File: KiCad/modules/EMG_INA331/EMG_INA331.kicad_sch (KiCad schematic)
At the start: 34 parts, among them J10 Conn_01x01_Pin, J13 Conn_01x01_Pin, J14 Conn_01x01_Pin, J15 Conn_01x01_Pin, J6 Conn_01x01_Pin, J7 Conn_01x01_Pin, J8 Conn_01x01_Pin, J9 Conn_01x01_Pin, U1 TLV9044IPWR, U2 AP2112K-3.3TRG1, U3 INA350ABSIDSGR_C4370677

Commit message: INA331 IMUICM
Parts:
- removed C6: 1uF, Capacitor_SMD:C_0402_1005Metric, symbol Device:C
- removed R1, R10, R12, R14: R, Resistor_SMD:R_0201_0603Metric, symbol Device:R
- removed U1: TLV9044IPWR, 00_lcsc:TSSOP-14_L5.0-W4.4-P0.65-LS6.4-BL, symbol 00_lcsc:TLV9044IPWR
- removed U2: AP2112K-3.3TRG1, 00_custom-footprints:SOT95P285X140-5N, symbol 00_custom:AP2112K-3.3TRG1
- added C14: 100n, Capacitor_SMD:C_0402_1005Metric, symbol Device:C
- added C15: 1u, Capacitor_SMD:C_0402_1005Metric, symbol Device:C
- added C3: 10nF, Capacitor_SMD:C_0402_1005Metric, symbol Device:C
- added C7: 1uF, Capacitor_SMD:C_0402_1005Metric, symbol Device:C
- added C9: 100nF, Capacitor_SMD:C_0402_1005Metric, symbol Device:C
- added J10, J9: Conn_01x01_Pin, 00_custom-footprints:PinHeader_1x01_P1.27mm_Vertical, symbol Connector:Conn_01x01_Pin
- added R4, R5: 4k, Resistor_SMD:R_0402_1005Metric, symbol Device:R
- added R6, R7: 10k, Resistor_SMD:R_0402_1005Metric, symbol Device:R
- added TP1, TP2, TP3: TestPoint, 00_custom-footprints:TestPoint_Pad_D1.0mm, symbol 00_custom:TestPoint
- added U2, U4: OPA333, 00_lcsc:SOT-23-5_L2.9-W1.6-P0.95-LS2.8-BR, symbol 00_lcsc:OPA333M5_TR
- added U3: AP2112K-3.3TRG1, 00_lcsc:SOT-25-5_L2.9-W1.6-P0.95-LS2.8-BL, symbol 00_lcsc:AP2112K-3.3TRG1
- added U5: CJ432, 00_lcsc:SOT-23-3_L2.9-W1.3-P1.90-LS2.4-BR, symbol 00_lcsc:CJ432
- added U6: LIS3DHTR, 00_lcsc:LGA-16_L3.0-W3.0-P0.50-TL, symbol 00_lcsc:LIS3DHTR
- C1: renamed from C11; value 1uF -> 10uF
- C12: renamed from C1; value 1uF -> 100nF
- C2: renamed from C12; value 1uF -> 100nF
- C4, C5: value 1uF -> 100pF
- C5: footprint Capacitor_SMD:C_0201_0603Metric -> Capacitor_SMD:C_0402_1005Metric
- J10, J13, J14, J15, J6, J7, J8, J9: footprint Connector_PinHeader_1.27mm:PinHeader_1x01_P1.27mm_Vertical -> 00_custom-footprints:PinHeader_1x01_P1.27mm_Vertical
- R1: renamed from R5; value R -> 2k; footprint Resistor_SMD:R_0201_0603Metric -> Resistor_SMD:R_0402_1005Metric
- R10: renamed from R11; value R -> 1k; footprint Resistor_SMD:R_0201_0603Metric -> Resistor_SMD:R_0402_1005Metric
- R11: renamed from R9; value R -> 100k; footprint Resistor_SMD:R_0201_0603Metric -> Resistor_SMD:R_0402_1005Metric
- R12: renamed from R4; value R -> 1k; footprint Resistor_SMD:R_0201_0603Metric -> Resistor_SMD:R_0402_1005Metric
- R2: renamed from R3; value R -> 10k; footprint Resistor_SMD:R_0201_0603Metric -> Resistor_SMD:R_0402_1005Metric
- R3: renamed from R6; value R -> 330; footprint Resistor_SMD:R_0201_0603Metric -> Resistor_SMD:R_0402_1005Metric
- R8: renamed from R2; value R -> 100k; footprint Resistor_SMD:R_0201_0603Metric -> Resistor_SMD:R_0402_1005Metric
- R9: renamed from R7; value R -> 1M; footprint Resistor_SMD:R_0201_0603Metric -> Resistor_SMD:R_0402_1005Metric
- U1: renamed from U3; value INA350ABSIDSGR_C4370677 -> INA350ABSIDSGR
- renumbered C3 to C10, C10 to C13, C14 to C8
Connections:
- net +3.3V: now also C14.1, C15.1, U3.1 (VIN), U3.3 (EN), U6.1 (VDD_IO)
- net +3.3VA: now also C12.1, R3.1, U1.7 (V+), C7.2, C9.1, U2.2 (V-), U3.5 (VOUT), U4.5 (V+), U6.14 (VDD)
- net CSB: now also U6.8 (CS)
- net GND: now also C1.2, C12.2, C2.2, R12.2, R2.2, U1.4 (V–), C14.2, C15.2, C7.1, C9.2, U2.5 (V+), U3.2 (GND), U4.2 (V-), U5.3 (A), U6.10 (RES), U6.12 (GND), U6.5 (GND)
- net MISO: now also U6.7 (SDO/SA0)
- net MOSI: now also U6.6 (SDA/SDI/SDO)
- net SCLK: now also U6.4 (SCL/SPC)
- net Vref: now reaches C1.1
- net Vref: now also C2.1, C4.2, C5.1, R1.1, R10.1, R3.2, R9.2, TP3.1, U2.3 (+IN), U5.2 (K)
- net at R2.1: now also R1.2, U5.1 (R)
- net at R8.1: now also C8.2, U2.4 (-IN)
- net OUT_INA: now reaches R8.2
- net OUT_INA: now also C10.1, U1.6 (OUT), R7.2
- net at U1.1 (GS): now also R6.2, R7.1
- net IN+: now reaches U1.2 (IN–)
- net IN+: now also C4.1, C3.1, R4.2
- net IN-: now reaches U1.3 (IN+)
- net IN-: now also C5.2, C3.2, R5.2
- net REF: now reaches U1.5 (REF)
- net REF: now also C8.1, R6.1, U2.1 (OUT)
- net at R11.1: now also C13.1, R10.2, U4.4 (-IN)
- net OUT1: now reaches R11.2
- net OUT1: now also C13.2, R12.1, TP1.1, U4.1 (OUT), U6.16 (ADC1)
- net at C10.2: now also R9.1, U4.3 (+IN)
- new net ADC2: TP2.1, U6.15 (ADC2)
- new net PROB+: J10.1 (Pin_1), R4.1
- new net PROB-: J9.1 (Pin_1), R5.1
- no-connect marks 1 -> 5
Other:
- moved on the sheet: C1, C10, C12, C13, C2, C8, R1, R10, R11, R12, R2, R3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

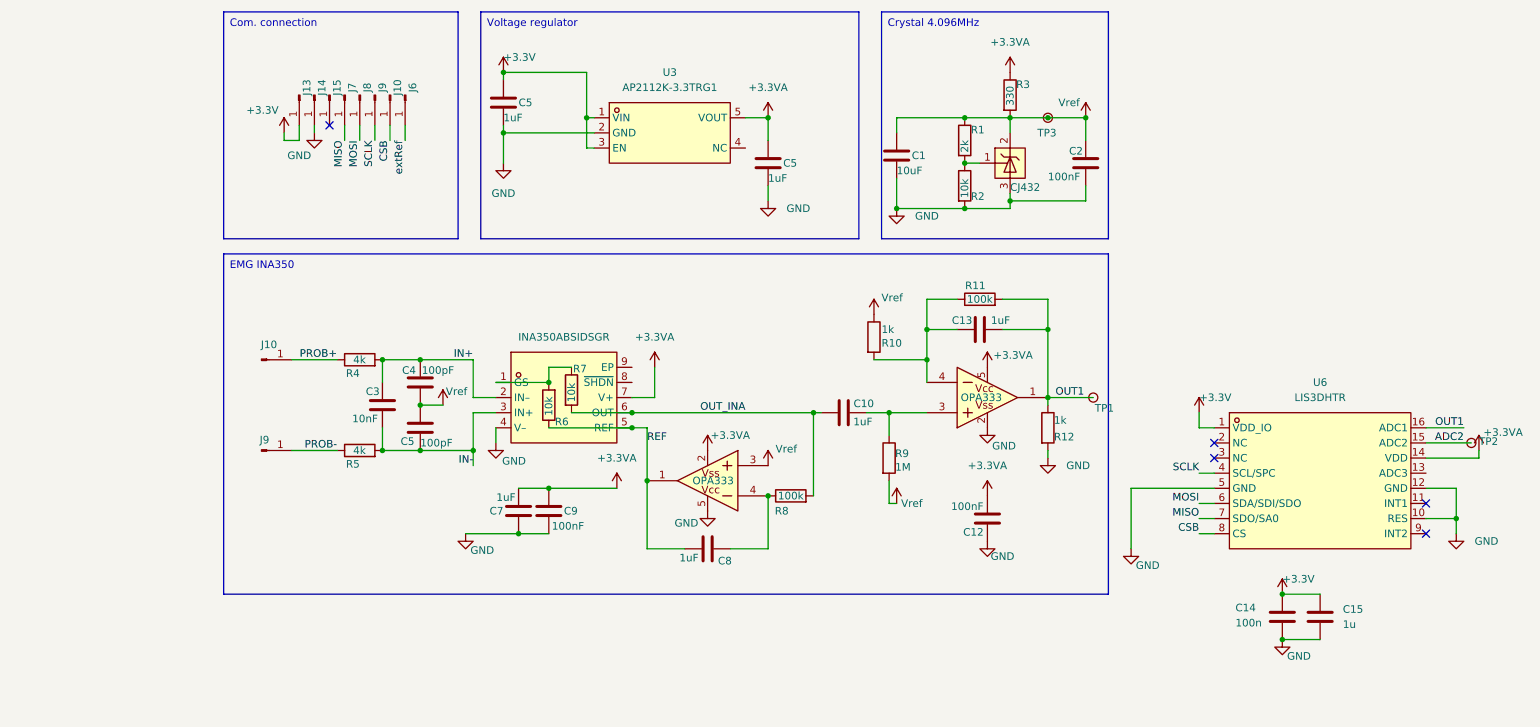
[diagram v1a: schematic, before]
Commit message: refactor and fixing most of the modules
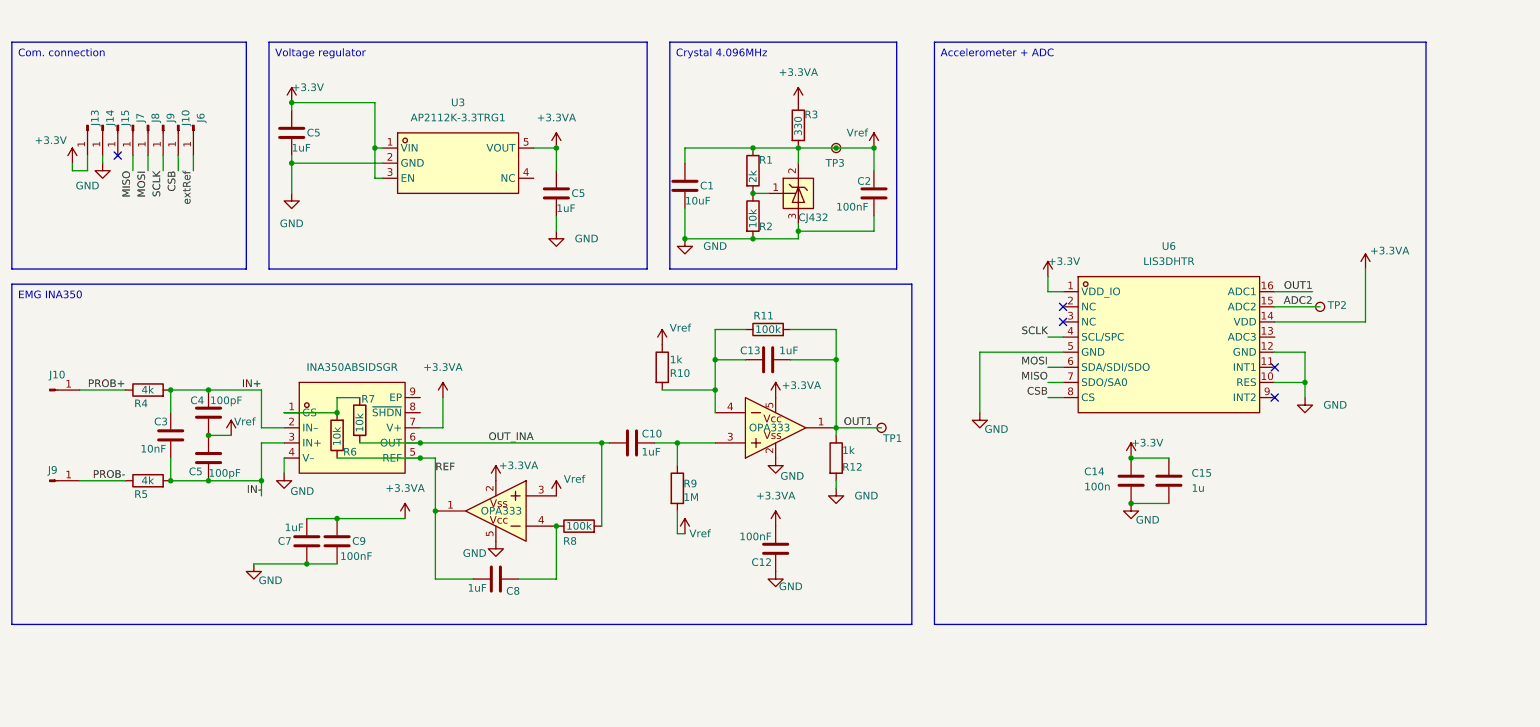
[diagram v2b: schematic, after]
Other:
- company: (none) -> Aightech
- title: EMG DAQ ADS129 -> EMG INA331
- moved on the sheet: C1, C10, C12, C13, C14, C15, C2, C3, C4, C5, C7, C8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

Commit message: cleaned all modules + production files
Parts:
- J10, J9: now not fitted; now left out of the parts list
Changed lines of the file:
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@@
 		(unit 1)
 		(exclude_from_sim no)
-		(in_bom yes)
-		(on_board yes)
-		(dnp no)
+		(in_bom no)
+		(on_board yes)
+		(dnp yes)
 		(property "Reference" "J9"
 			(at 37.338 118.872 0)
@@
 		(unit 1)
 		(exclude_from_sim no)
-		(in_bom yes)
-		(on_board yes)
-		(dnp no)
+		(in_bom no)
+		(on_board yes)
+		(dnp yes)
 		(property "Reference" "J10"
 			(at 38.1 102.87 0)

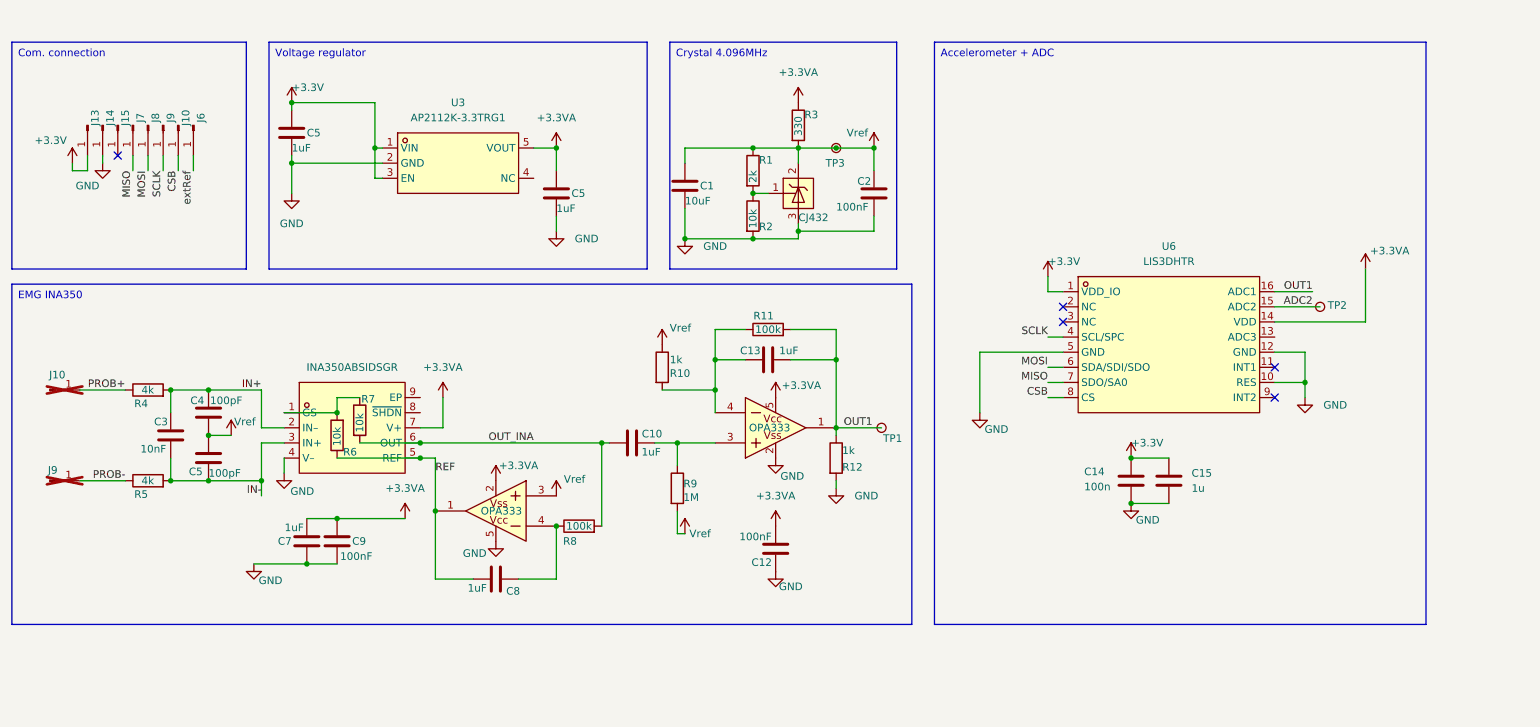
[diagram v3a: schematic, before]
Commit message: fixed INA331 wrong package and add ext ref
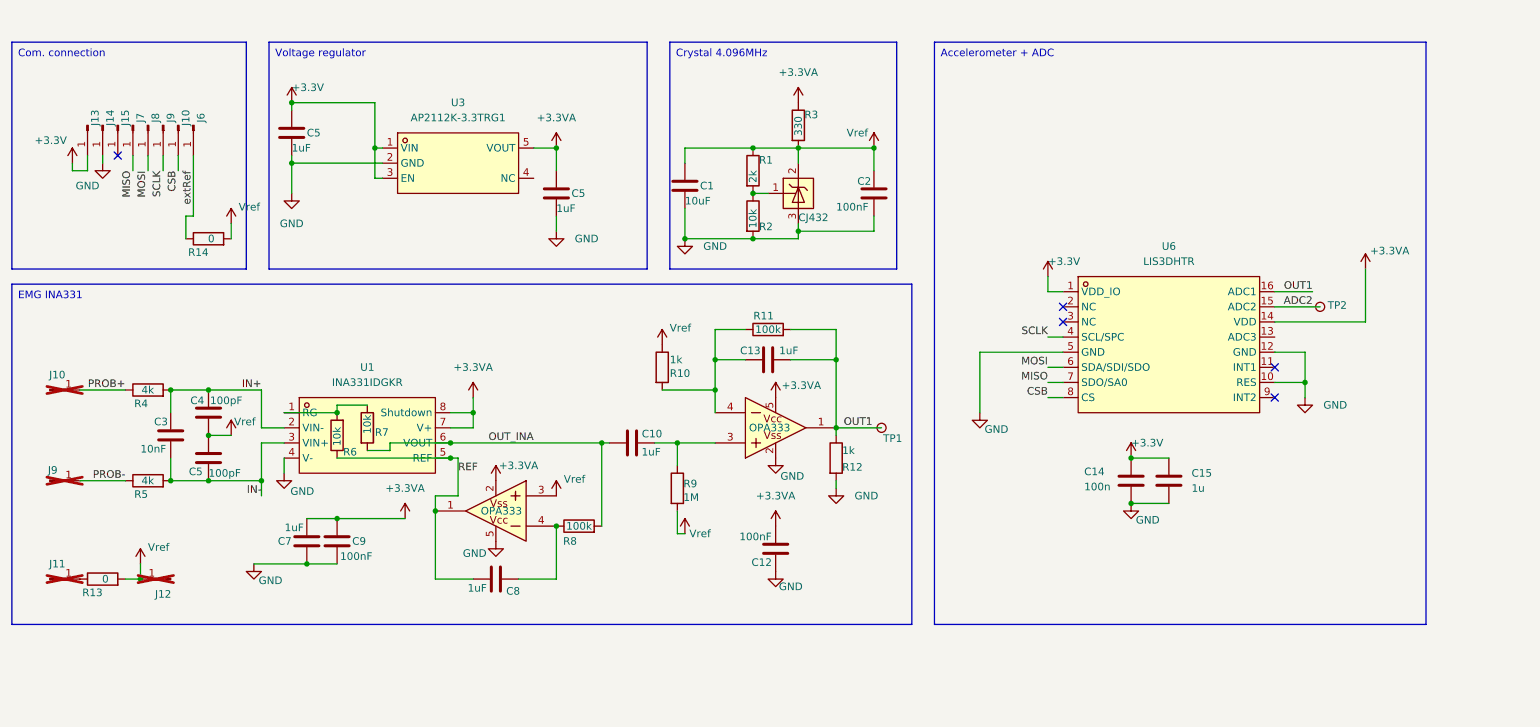
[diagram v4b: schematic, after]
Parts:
- removed TP3: TestPoint, 00_custom-footprints:TestPoint_Pad_D1.0mm, symbol 00_custom:TestPoint
- removed U1: INA350ABSIDSGR, 00_lcsc:WSON-8_L2.0-W2.0-P0.50-TL-EP, symbol 00_lcsc:INA350ABSIDSGR_C4370677
- added J11, J12: Conn_01x01_Pin, 00_custom-footprints:PinHeader_1x01_P1.27mm_Vertical, symbol Connector:Conn_01x01_Pin
- added R13, R14: 0, Resistor_SMD:R_0402_1005Metric, symbol Device:R
- added U1: INA331IDGKR, 00_lcsc:VSSOP-8_L3.0-W3.0-P0.65-LS5.0-BL, symbol 00_lcsc:INA331IDGKR
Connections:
- net +3.3VA: now also U1.7 (V+), U1.8 (Shutdown)
- net GND: now also U1.4 (V-)
- net IN+: now also U1.2 (VIN-)
- net IN-: now also U1.3 (VIN+)
- net OUT_INA: now also U1.6 (VOUT)
- net REF: now also U1.5 (REF)
- net Vref: now also J12.1 (Pin_1), R13.2, R14.2
- net extRef: now also R14.1
- net at R6.2, R7.1: now also U1.1 (RG)
- new net: J11.1 (Pin_1), R13.1
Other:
- moved on the sheet: R7

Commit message: renamed SPI buses
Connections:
- net MISO renamed POCI
- net MOSI renamed PICO
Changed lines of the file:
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@@
 		)
 	)
-	(label "MOSI"
+	(label "PICO"
 		(at 53.34 68.58 270)
 		(fields_autoplaced yes)
@@
 		)
 	)
-	(label "MISO"
+	(label "POCI"
 		(at 204.47 104.14 180)
 		(fields_autoplaced yes)
@@
 		)
 	)
-	(label "MOSI"
+	(label "PICO"
 		(at 204.47 101.6 180)
 		(fields_autoplaced yes)
@@
 		)
 	)
-	(label "MISO"
+	(label "POCI"
 		(at 50.8 68.58 270)
 		(fields_autoplaced yes)
